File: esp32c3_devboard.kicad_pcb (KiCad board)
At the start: 2 copper layers, 40.6 x 25.4 mm, 55 parts, among them J1 Conn_01x15_Male, J2 Conn_01x15_Male, J3 Micro_USB, Q1 S8050, Q2 S8050, SW1 BOOT, SW2 RST, U1 USB2514B_Bi, U2 CH340X, U3 ESP32-C3-MINI-1, U4 AMS1117-3.3, U5 SRV05-4, Y1 24MHz

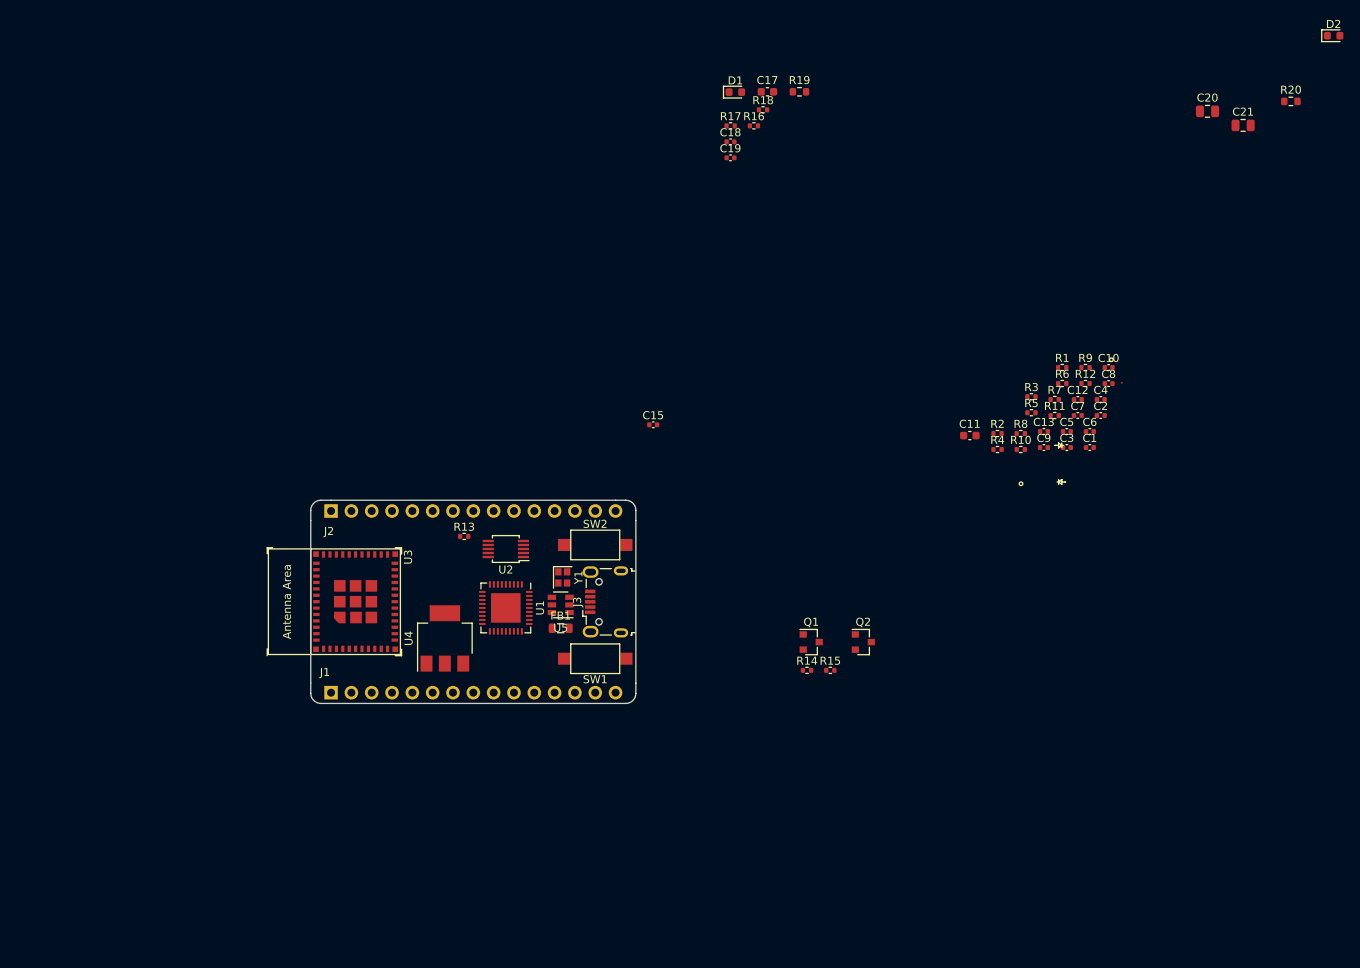
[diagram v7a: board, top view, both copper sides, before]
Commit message: Use ESP32-C3-WROOM-02 module
Signed-off-by: Tomislav Milkovic <tomislav.milkovic95@gmail.com>
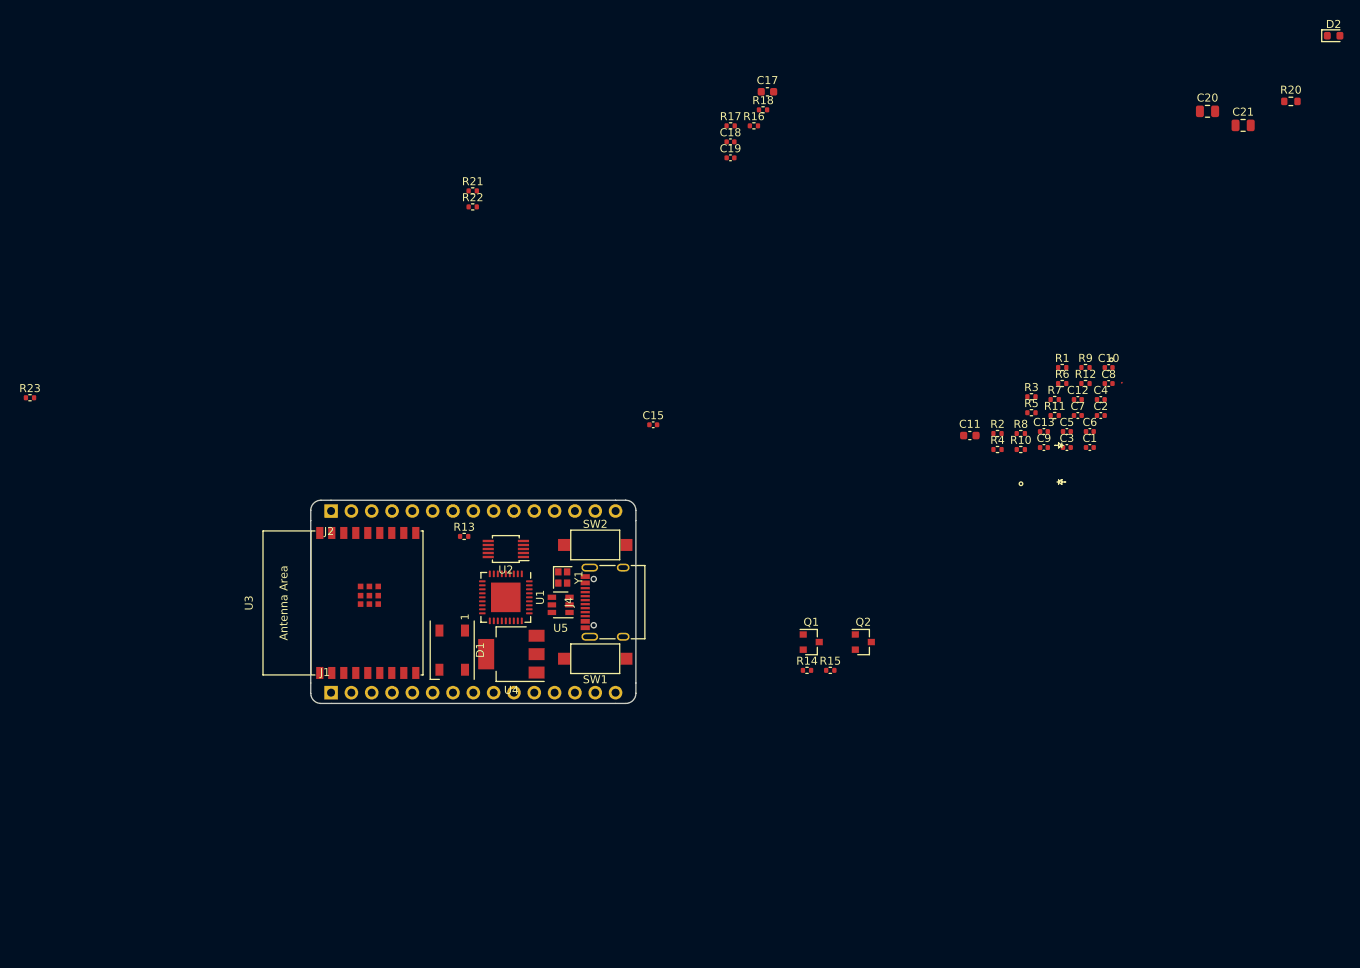
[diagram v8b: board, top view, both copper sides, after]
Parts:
- removed FB1: 100Ω @ 100MHz, Inductor_SMD:L_0805_2012Metric
- removed J3: Micro_USB, Connector_USB:USB_Micro-B_Wuerth_629105150521
- removed R19: 470Ω, Resistor_SMD:R_0603_1608Metric
- added J4: USB_C_Receptacle_USB2.0, Connector_USB:USB_C_Receptacle_XKB_U262-16XN-4BVC11, F.Cu at (147.2, 124.5)
- added R21: 5K1, Resistor_SMD:R_0402_1005Metric, F.Cu at (129.5, 73.1)
- added R22: 5K1, Resistor_SMD:R_0402_1005Metric, F.Cu at (129.5, 75.1)
- added R23: 10M, Resistor_SMD:R_0402_1005Metric, F.Cu at (74.1, 98.9)
- D1: value USR_LED -> WS2812B; footprint LED_SMD:LED_0603_1608Metric -> LED_SMD:LED_WS2812B_PLCC4_5.0x5.0mm_P3.2mm
- U3: value ESP32-C3-MINI-1 -> ESP32-C3-WROOM-02; footprint Espressif:ESP32-C3-MINI-1 -> Espressif:ESP32-C3-WROOM-02
- moved D1 78.2 mm to (126.9, 130.5), turned to 270 degrees
- moved U4 8.55 mm to (134.3, 131.0), turned to 180 degrees
- moved U1 1.32 mm to (133.6, 123.9)
- moved U3 0.36 mm to (114.5, 124.6)
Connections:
- net /ESP32-C3 module/UART_DTR renamed /ESP32-C3 module/ESP32_UART_DTR
- net /ESP32-C3 module/UART_RTS renamed /ESP32-C3 module/ESP32_UART_RTS
- D1 pad 1: GND -> +5V
- D1 pad 2: /ESP32-C3 module/USR_LED_A -> (no net)
- J1 pad 10: /ESP32-C3 module/GPIO1 -> GND
- J1 pad 11: /ESP32-C3 module/GPIO10 -> /ESP32-C3 module/GPIO8
- J1 pad 12: GND -> /ESP32-C3 module/GPIO9
- J1 pad 4: /ESP32-C3 module/GPIO2 -> /ESP32-C3 module/~RST
- J1 pad 5: /ESP32-C3 module/GPIO3 -> GND
- J1 pad 6: GND -> /ESP32-C3 module/GPIO4
- J1 pad 7: /ESP32-C3 module/~RST -> /ESP32-C3 module/GPIO5
- J1 pad 8: GND -> /ESP32-C3 module/GPIO6
- J1 pad 9: /ESP32-C3 module/GPIO0 -> /ESP32-C3 module/GPIO7
- J2 pad 10: /ESP32-C3 module/GPIO5 -> /ESP32-C3 module/ESP32_UART_TXD
- J2 pad 11: /ESP32-C3 module/GPIO4 -> GND
- J2 pad 12: GND -> /USB hub/DOWNSTREAM_USB2_D-
- J2 pad 13: /USB hub/DOWNSTREAM_USB2_D- -> /USB hub/DOWNSTREAM_USB2_D+
- J2 pad 14: /USB hub/DOWNSTREAM_USB2_D+ -> GND
- J2 pad 2: /USB-UART bridge/UART_RXD -> /ESP32-C3 module/GPIO0
- J2 pad 3: /ESP32-C3 module/UART_RXD -> /ESP32-C3 module/GPIO1
- J2 pad 4: GND -> /ESP32-C3 module/GPIO2
- J2 pad 5: /ESP32-C3 module/GPIO9 -> /ESP32-C3 module/GPIO3
- J2 pad 6: /ESP32-C3 module/GPIO8 -> GND
- J2 pad 7: GND -> /ESP32-C3 module/GPIO10
- J2 pad 8: /ESP32-C3 module/GPIO7 -> GND
- J2 pad 9: /ESP32-C3 module/GPIO6 -> /ESP32-C3 module/ESP32_UART_RXD
- U1 pad 30: /USB hub/UPSTREAM_USB_D- -> /USB connector and power supply/CONN_USB_D-
- U1 pad 31: /USB hub/UPSTREAM_USB_D+ -> /USB connector and power supply/CONN_USB_D+
- U2 pad 8: /ESP32-C3 module/UART_RXD -> /ESP32-C3 module/ESP32_UART_RXD
- U2 pad 9: /USB-UART bridge/UART_RXD -> /ESP32-C3 module/ESP32_UART_TXD
- U3 pad 1: GND -> +3V3
- U3 pad 10: (no net) -> /ESP32-C3 module/GPIO10
- U3 pad 11: GND -> /ESP32-C3 module/ESP32_UART_RXD
- U3 pad 12: /ESP32-C3 module/GPIO0 -> /ESP32-C3 module/ESP32_UART_TXD
- U3 pad 13: /ESP32-C3 module/GPIO1 -> /USB hub/DOWNSTREAM_USB2_D-
- U3 pad 14: GND -> /USB hub/DOWNSTREAM_USB2_D+
- U3 pad 15: (no net) -> /ESP32-C3 module/GPIO3
- U3 pad 16: /ESP32-C3 module/GPIO10 -> /ESP32-C3 module/GPIO2
- U3 pad 17: (no net) -> /ESP32-C3 module/GPIO1
- U3 pad 18: /ESP32-C3 module/GPIO4 -> /ESP32-C3 module/GPIO0
- U3 pad 19: /ESP32-C3 module/GPIO5 -> GND
- U3 pad 2: GND -> /ESP32-C3 module/~RST
- U3 pad 3: +3V3 -> /ESP32-C3 module/GPIO4
- U3 pad 4: (no net) -> /ESP32-C3 module/GPIO5
- U3 pad 5: /ESP32-C3 module/GPIO2 -> /ESP32-C3 module/GPIO6
- U3 pad 6: /ESP32-C3 module/GPIO3 -> /ESP32-C3 module/GPIO7
- U3 pad 7: (no net) -> /ESP32-C3 module/GPIO8
- U3 pad 8: /ESP32-C3 module/~RST -> /ESP32-C3 module/GPIO9
- U3 pad 9: (no net) -> GND
- U5 pad 1: /USB hub/UPSTREAM_USB_D- -> /USB connector and power supply/USB_D-
- U5 pad 3: /USB hub/UPSTREAM_USB_D+ -> /USB connector and power supply/USB_D+
- U5 pad 4: /USB hub/UPSTREAM_USB_D+ -> /USB connector and power supply/USB_D+
- U5 pad 6: /USB hub/UPSTREAM_USB_D- -> /USB connector and power supply/USB_D-
